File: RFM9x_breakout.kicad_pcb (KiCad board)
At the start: 2 copper layers, 22.9 x 20.3 mm, 6 parts, among them J1 Conn_01x08_Male, J2 Conn_01x08_Male, U2 RFM92/95/96/97/98

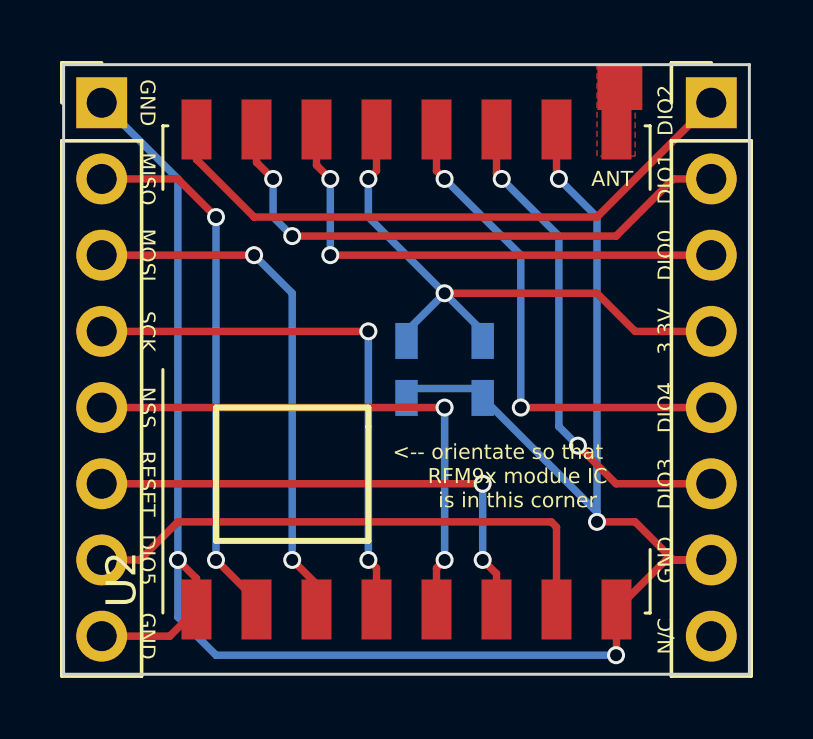
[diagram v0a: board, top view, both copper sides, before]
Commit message: increase font size of pin labels
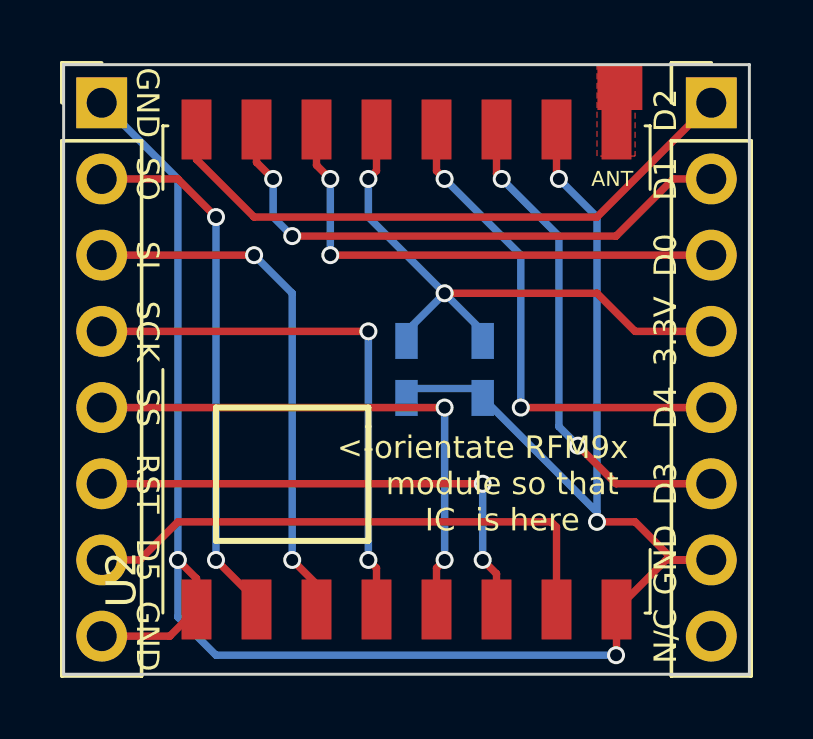
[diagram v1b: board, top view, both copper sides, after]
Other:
- board text added: "<-orientate RFM9x module so that IC is here"
- board text added: "D0"
- board text added: "D1"
- board text added: "D2"
- board text added: "D3"
- board text added: "D4"
- board text added: "D5"
- board text added: "RFM9x breakout V1.0.1 2018-05-07 Joe Desbonnet jdesbonnet@gmail.com"
- board text added: "RST"
- board text added: "SI"
- board text added: "SO"
- board text added: "SS"
- board text removed: "<-- orientate so that RFM9x module IC is in this corner"
- board text removed: "DIO0"
- board text removed: "DIO1"
- board text removed: "DIO2"
- board text removed: "DIO3"
- board text removed: "DIO4"
- board text removed: "DIO5"
- board text removed: "MISO"
- board text removed: "MOSI"
- board text removed: "NSS"
- board text removed: "RESET"
- board text removed: "RFM9x breakout V1.0.0 2018-04-15 Joe Desbonnet jdesbonnet@gmail.com"
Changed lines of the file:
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@@
-(kicad_pcb (version 4) (host pcbnew 4.0.7-e2-6376~58~ubuntu15.04.1)
+(kicad_pcb (version 4) (host pcbnew 4.0.2+dfsg1-stable)
   (general
     (links 21)
@@
     (pad 1 smd rect (at 0 0) (size 1.5 1.5) (layers F.Cu F.Mask))
   )
-  (gr_text "<-- orientate so that\n      RFM9x module IC \n      is in this corner" (at 152.908 108.966) (layer F.SilkS)
-    (effects (font (size 0.5 0.5) (thickness 0.1)))
-  )
-  (gr_text DIO5 (at 141.224 111.76 270) (layer F.SilkS)
-    (effects (font (size 0.5 0.5) (thickness 0.1)))
+  (gr_text "<-orientate RFM9x \n    module so that \n    IC  is here" (at 152.4 109.22) (layer F.SilkS)
+    (effects (font (size 0.75 0.75) (thickness 0.1)))
+  )
+  (gr_text D5 (at 141.224 111.76 270) (layer F.SilkS)
+    (effects (font (size 0.75 0.75) (thickness 0.1)))
   )
   (gr_text N/C (at 158.496 114.3 90) (layer B.SilkS)
+    (effects (font (size 0.75 0.75) (thickness 0.1)) (justify mirror))
+  )
+  (gr_text D2 (at 158.496 96.774 90) (layer B.SilkS)
+    (effects (font (size 0.75 0.75) (thickness 0.1)) (justify mirror))
+  )
+  (gr_text D1 (at 158.496 99.06 90) (layer B.SilkS)
+    (effects (font (size 0.75 0.75) (thickness 0.1)) (justify mirror))
+  )
+  (gr_text D0 (at 158.496 101.6 90) (layer B.SilkS)
+    (effects (font (size 0.75 0.75) (thickness 0.1)) (justify mirror))
+  )
+  (gr_text D4 (at 158.496 106.68 90) (layer B.SilkS)
+    (effects (font (size 0.75 0.75) (thickness 0.1)) (justify mirror))
+  )
+  (gr_text D3 (at 158.496 109.22 90) (layer B.SilkS)
     (effects (font (size 0.5 0.5) (thickness 0.1)) (justify mirror))
   )
-  (gr_text DIO2 (at 158.496 96.774 90) (layer B.SilkS)
+  (gr_text GND (at 158.496 111.76 90) (layer B.SilkS)
+    (effects (font (size 0.75 0.75) (thickness 0.1)) (justify mirror))
+  )
+  (gr_text N/C (at 158.496 114.3 90) (layer F.SilkS)
+    (effects (font (size 0.75 0.75) (thickness 0.1)))
+  )
+  (gr_text RST (at 141.224 109.22 270) (layer B.SilkS)
+    (effects (font (size 0.75 0.75) (thickness 0.1)) (justify mirror))
+  )
+  (gr_text SS (at 141.224 106.68 270) (layer B.SilkS)
     (effects (font (size 0.5 0.5) (thickness 0.1)) (justify mirror))
   )
-  (gr_text DIO1 (at 158.496 99.06 90) (layer B.SilkS)
+  (gr_text "SCK\n" (at 141.224 104.14 270) (layer B.SilkS)
+    (effects (font (size 0.75 0.75) (thickness 0.1)) (justify mirror))
+  )
+  (gr_text SI (at 141.224 101.6 270) (layer B.SilkS)
     (effects (font (size 0.5 0.5) (thickness 0.1)) (justify mirror))
   )
-  (gr_text DIO0 (at 158.496 101.6 90) (layer B.SilkS)
-    (effects (font (size 0.5 0.5) (thickness 0.1)) (justify mirror))
-  )
-  (gr_text DIO4 (at 158.496 106.68 90) (layer B.SilkS)
-    (effects (font (size 0.5 0.5) (thickness 0.1)) (justify mirror))
-  )
-  (gr_text DIO3 (at 158.496 109.22 90) (layer B.SilkS)
-    (effects (font (size 0.5 0.5) (thickness 0.1)) (justify mirror))
-  )
-  (gr_text GND (at 158.496 111.76 90) (layer B.SilkS)
-    (effects (font (size 0.5 0.5) (thickness 0.1)) (justify mirror))
-  )
-  (gr_text N/C (at 158.496 114.3 90) (layer F.SilkS)
-    (effects (font (size 0.5 0.5) (thickness 0.1)))
-  )
-  (gr_text RESET (at 141.224 109.22 270) (layer B.SilkS)
-    (effects (font (size 0.5 0.5) (thickness 0.1)) (justify mirror))
-  )
-  (gr_text NSS (at 141.224 106.68 270) (layer B.SilkS)
-    (effects (font (size 0.5 0.5) (thickness 0.1)) (justify mirror))
-  )
-  (gr_text "SCK\n" (at 141.224 104.14 270) (layer B.SilkS)
-    (effects (font (size 0.5 0.5) (thickness 0.1)) (justify mirror))
-  )
-  (gr_text MOSI (at 141.224 101.6 270) (layer B.SilkS)
-    (effects (font (size 0.5 0.5) (thickness 0.1)) (justify mirror))
-  )
-  (gr_text MISO (at 141.224 99.06 270) (layer B.SilkS)
-    (effects (font (size 0.5 0.5) (thickness 0.1)) (justify mirror))
+  (gr_text SO (at 141.224 99.06 270) (layer B.SilkS)
+    (effects (font (size 0.75 0.75) (thickness 0.1)) (justify mirror))
   )
   (gr_text GND (at 141.224 96.52 270) (layer B.SilkS)
-    (effects (font (size 0.5 0.5) (thickness 0.1)) (justify mirror))
+    (effects (font (size 0.75 0.75) (thickness 0.1)) (justify mirror))
   )
   (gr_text GND (at 141.224 114.3 270) (layer B.SilkS)
-    (effects (font (size 0.5 0.5) (thickness 0.1)) (justify mirror))
+    (effects (font (size 0.75 0.75) (thickness 0.1)) (justify mirror))
   )
   (gr_text ANT (at 156.718 99.06) (layer F.SilkS)
@@
   )
   (gr_text 3.3V (at 158.496 104.14 90) (layer B.SilkS)
-    (effects (font (size 0.5 0.5) (thickness 0.1)) (justify mirror))
-  )
-  (gr_text "RFM9x breakout\nV1.0.0  2018-04-15\nJoe Desbonnet\njdesbonnet@gmail.com" (at 149.352 110.49) (layer B.SilkS)
-    (effects (font (size 0.8 0.8) (thickness 0.2)) (justify mirror))
-  )
-  (gr_text DIO2 (at 158.496 96.774 90) (layer F.SilkS)
-    (effects (font (size 0.5 0.5) (thickness 0.1)))
-  )
-  (gr_text DIO1 (at 158.496 99.06 90) (layer F.SilkS)
-    (effects (font (size 0.5 0.5) (thickness 0.1)))
-  )
-  (gr_text DIO0 (at 158.496 101.6 90) (layer F.SilkS)
-    (effects (font (size 0.5 0.5) (thickness 0.1)))
+    (effects (font (size 0.75 0.75) (thickness 0.1)) (justify mirror))
+  )
+  (gr_text "RFM9x breakout\nV1.0.1  2018-05-07\nJoe Desbonnet\njdesbonnet@gmail.com" (at 149.352 110.49) (layer B.SilkS)
+    (effects (font (size 0.85 0.85) (thickness 0.2)) (justify mirror))
+  )
+  (gr_text D2 (at 158.496 96.774 90) (layer F.SilkS)
+    (effects (font (size 0.75 0.75) (thickness 0.1)))
+  )
+  (gr_text D1 (at 158.496 99.06 90) (layer F.SilkS)
+    (effects (font (size 0.75 0.75) (thickness 0.1)))
+  )
+  (gr_text D0 (at 158.496 101.6 90) (layer F.SilkS)
+    (effects (font (size 0.75 0.75) (thickness 0.1)))
   )
   (gr_text 3.3V (at 158.496 104.14 90) (layer F.SilkS)
-    (effects (font (size 0.5 0.5) (thickness 0.1)))
-  )
-  (gr_text DIO4 (at 158.496 106.68 90) (layer F.SilkS)
-    (effects (font (size 0.5 0.5) (thickness 0.1)))
-  )
-  (gr_text DIO3 (at 158.496 109.22 90) (layer F.SilkS)
-    (effects (font (size 0.5 0.5) (thickness 0.1)))
+    (effects (font (size 0.75 0.75) (thickness 0.1)))
+  )
+  (gr_text D4 (at 158.496 106.68 90) (layer F.SilkS)
+    (effects (font (size 0.75 0.75) (thickness 0.1)))
+  )
+  (gr_text D3 (at 158.496 109.22 90) (layer F.SilkS)
+    (effects (font (size 0.75 0.75) (thickness 0.1)))
   )
   (gr_text GND (at 158.496 111.76 90) (layer F.SilkS)
-    (effects (font (size 0.5 0.5) (thickness 0.1)))
+    (effects (font (size 0.75 0.75) (thickness 0.1)))
   )
   (gr_text GND (at 141.224 114.3 270) (layer F.SilkS)
-    (effects (font (size 0.5 0.5) (thickness 0.1)))
-  )
-  (gr_text DIO5 (at 141.224 111.76 270) (layer B.SilkS)
-    (effects (font (size 0.5 0.5) (thickness 0.1)) (justify mirror))
-  )
-  (gr_text RESET (at 141.224 109.22 270) (layer F.SilkS)
-    (effects (font (size 0.5 0.5) (thickness 0.1)))
-  )
-  (gr_text NSS (at 141.224 106.68 270) (layer F.SilkS)
-    (effects (font (size 0.5 0.5) (thickness 0.1)))
+    (effects (font (size 0.75 0.75) (thickness 0.1)))
+  )
+  (gr_text D5 (at 141.224 111.76 270) (layer B.SilkS)
+    (effects (font (size 0.75 0.75) (thickness 0.1)) (justify mirror))
+  )
+  (gr_text RST (at 141.224 109.22 270) (layer F.SilkS)
+    (effects (font (size 0.75 0.75) (thickness 0.1)))
+  )
+  (gr_text SS (at 141.224 106.68 270) (layer F.SilkS)
+    (effects (font (size 0.75 0.75) (thickness 0.1)))
   )
   (gr_text "SCK\n" (at 141.224 104.14 270) (layer F.SilkS)
-    (effects (font (size 0.5 0.5) (thickness 0.1)))
-  )
-  (gr_text MOSI (at 141.224 101.6 270) (layer F.SilkS)
-    (effects (font (size 0.5 0.5) (thickness 0.1)))
-  )
-  (gr_text MISO (at 141.224 99.06 270) (layer F.SilkS)
-    (effects (font (size 0.5 0.5) (thickness 0.1)))
+    (effects (font (size 0.75 0.75) (thickness 0.1)))
+  )
+  (gr_text SI (at 141.224 101.6 270) (layer F.SilkS)
+    (effects (font (size 0.75 0.75) (thickness 0.1)))
+  )
+  (gr_text SO (at 141.224 99.06 270) (layer F.SilkS)
+    (effects (font (size 0.75 0.75) (thickness 0.1)))
   )
   (gr_text GND (at 141.224 96.52 270) (layer F.SilkS)
-    (effects (font (size 0.5 0.5) (thickness 0.1)))
+    (effects (font (size 0.75 0.75) (thickness 0.1)))
   )
   (gr_line (start 138.43 95.25) (end 161.29 95.25) (angle 90) (layer Edge.Cuts) (width 0.1))
